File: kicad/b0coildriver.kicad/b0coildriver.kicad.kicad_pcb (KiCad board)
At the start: 2 copper layers, 100.3 x 72.4 mm, 42 parts, among them J1 Vctrl, J2 PSU, J3 COIL, J4 Screw_Terminal_01x04, J5 ISense, U1 LM358, U2 OPA549T, U3 74HC04, U4 CMS2005

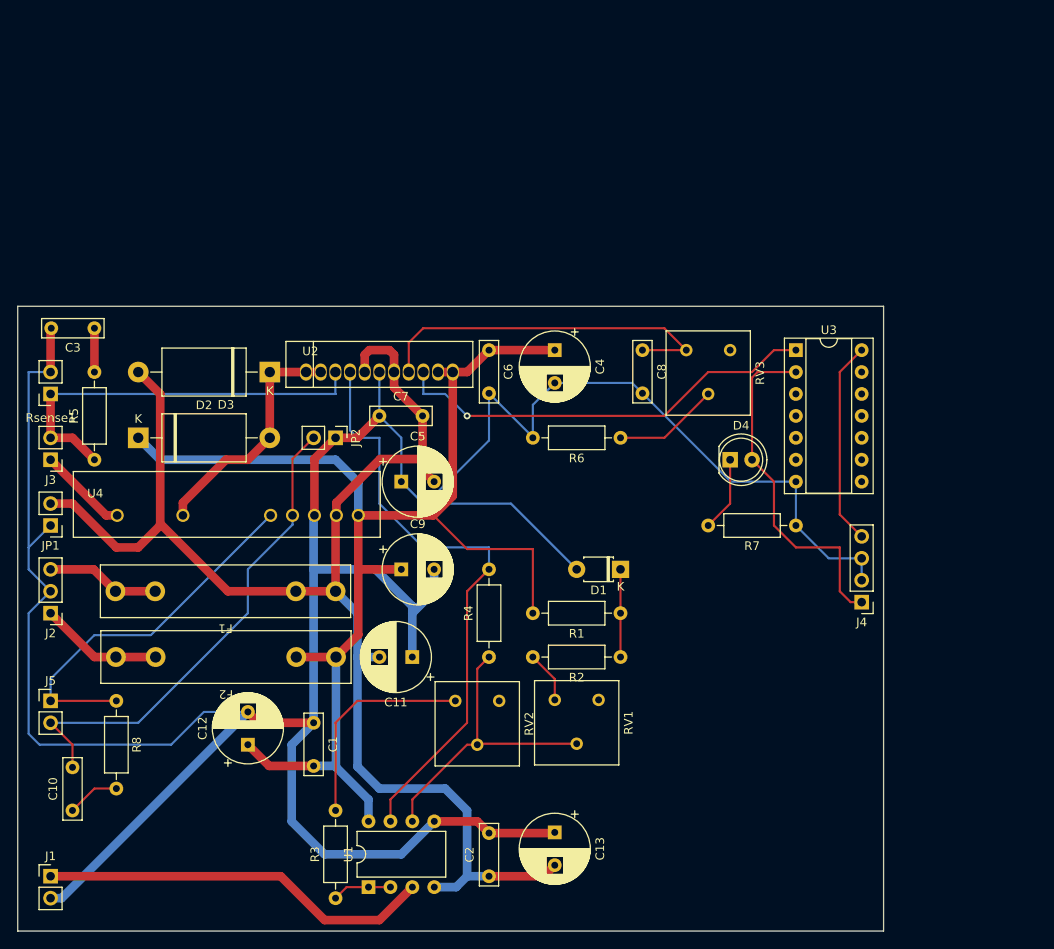
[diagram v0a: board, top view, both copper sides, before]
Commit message: Updated board layout to new feedback network
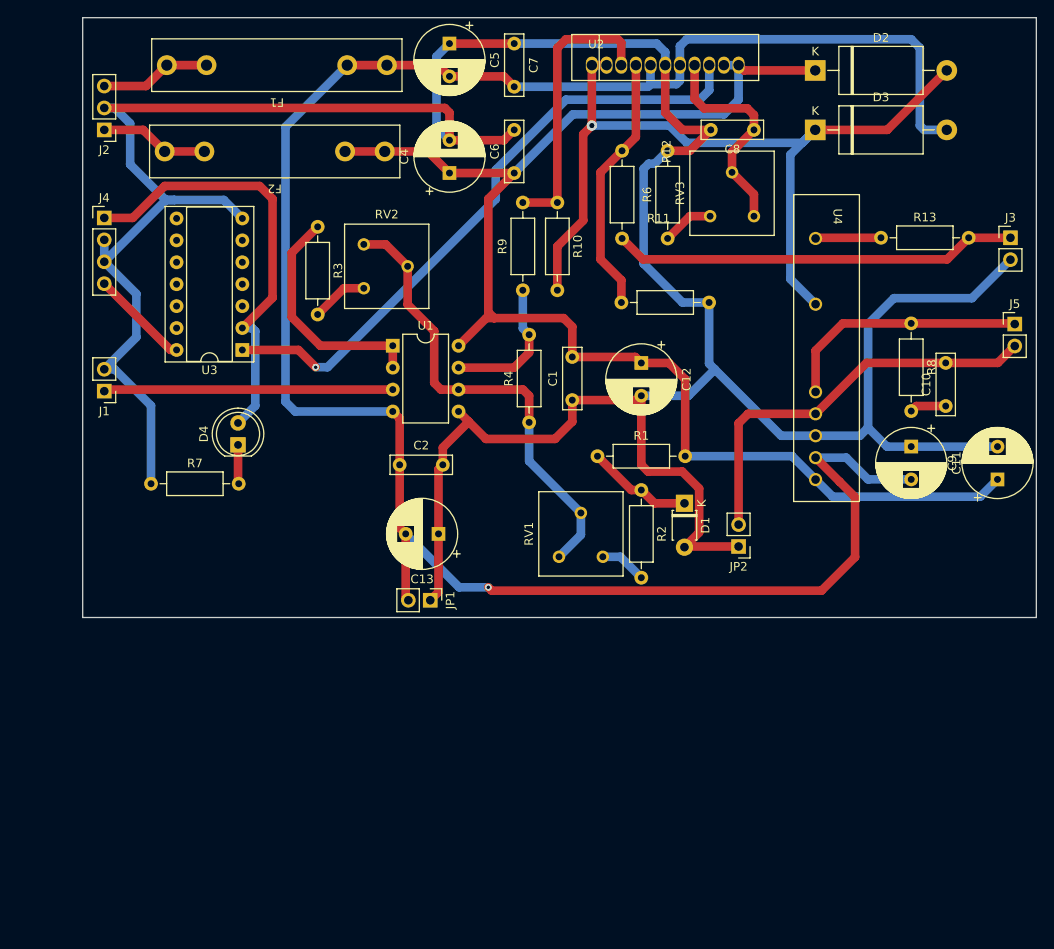
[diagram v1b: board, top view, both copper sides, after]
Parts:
- removed C3: 10nF, Capacitor_THT:C_Rect_L7.0mm_W2.0mm_P5.00mm
- removed R5: 10R, Resistor_THT:R_Axial_DIN0207_L6.3mm_D2.5mm_P10.16mm_Horizontal
- removed Rsense1: 1R, Connector_PinSocket_2.54mm:PinSocket_1x02_P2.54mm_Vertical
- added R10: 10k, Resistor_THT:R_Axial_DIN0207_L6.3mm_D2.5mm_P10.16mm_Horizontal, F.Cu at (140.0, 15.9)
- added R11: 20k, Resistor_THT:R_Axial_DIN0207_L6.3mm_D2.5mm_P10.16mm_Horizontal, F.Cu at (157.6, 27.5)
- added R12: 10k, Resistor_THT:R_Axial_DIN0207_L6.3mm_D2.5mm_P10.16mm_Horizontal, F.Cu at (147.5, 9.92)
- added R13: 1R, Resistor_THT:R_Axial_DIN0207_L6.3mm_D2.5mm_P10.16mm_Horizontal, F.Cu at (177.5, 20.0)
- added R9: 20k, Resistor_THT:R_Axial_DIN0207_L6.3mm_D2.5mm_P10.16mm_Horizontal, F.Cu at (136.0, 26.1)
- moved J5 119.9 mm to (193.0, 30.0)
- moved J3 114.2 mm to (192.5, 20.0), turned to 0 degrees
- moved C10 111.5 mm to (185.0, 39.5)
- moved R8 102.0 mm to (181.0, 29.9)
- moved J4 98.4 mm to (87.5, 17.7), turned to 0 degrees
- moved U4 96.6 mm to (175.0, 15.0), turned to -90 degrees
- moved D2 89.2 mm to (169.9, 0.61)
- moved R3 77.8 mm to (112.2, 18.7), turned to -90 degrees
- moved R7 74.9 mm to (92.9, 48.5), turned to 0 degrees
- moved C9 69.9 mm to (191.0, 48.0), turned to 90 degrees
- moved D3 69.1 mm to (169.9, 7.50), turned to 0 degrees
- moved U3 64.1 mm to (103.5, 33.0), turned to 180 degrees
- moved C12 63.5 mm to (149.7, 34.5), turned to -90 degrees
- moved U1 62.8 mm to (120.9, 32.5), turned to 0 degrees
- moved C11 62.7 mm to (181.0, 44.2), turned to -90 degrees
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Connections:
- C1 pad 1: GND -> VOut-
- C11 pad 1: GND -> VOut-
- C12 pad 2: GND -> VOut-
- C13 pad 1: GND -> VOut-
- C2 pad 2: GND -> VOut-
- C4 pad 2: GND -> VOut-
- C5 pad 1: GND -> VOut-
- C6 pad 2: GND -> VOut-
- C7 pad 1: GND -> VOut-
- C8 pad 2: GND -> VOut-
- C9 pad 2: GND -> VOut-
- D1 pad 2: GND -> VOut-
- J1 pad 2: GND -> VOut-
- J2 pad 2: GND -> VOut-
- J4 pad 2: GND -> VOut-
- J4 pad 3: GND -> VOut-
- JP1 pad 1: GND -> VOut-
- JP2 pad 1: GND -> VOut-
- R4 pad 1: Net-(R4-Pad1) -> Net-(RV1-Pad3)
- R6 pad 1: Net-(R6-Pad1) -> Net-(RV3-Pad3)
- R6 pad 2: GND -> VOut-
- R7 pad 1: GND -> VOut-
- RV1 pad 2: Net-(R4-Pad1) -> Net-(RV1-Pad3)
- RV1 pad 3: unconnected-(RV1-Pad3) -> Net-(RV1-Pad3)
- RV2 pad 2: Net-(R4-Pad1) -> Net-(RV1-Pad3)
- RV2 pad 3: unconnected-(RV2-Pad3) -> Net-(RV1-Pad3)
- RV3 pad 2: Net-(R6-Pad1) -> Net-(C8-Pad1)
- RV3 pad 3: unconnected-(RV3-Pad3) -> Net-(RV3-Pad3)
- U1 pad 5: GND -> VOut-
- U1 pad 6: Net-(R4-Pad1) -> Net-(RV1-Pad3)
- U2 pad 3: VOut- -> Net-(R10-Pad1)
- U2 pad 4: Net-(R4-Pad2) -> Net-(R11-Pad2)
- U2 pad 6: GND -> VOut-
- U3 pad 7: GND -> VOut-
- U4 pad 3: GND -> VOut-
- U4 pad 7: VOut+ -> Net-(R13-Pad1)
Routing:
- net GND: track 353.1 -> 0.00 mm
- net VOut-: track 46.8 -> 366.8 mm
- net -15V: track 164.5 -> 246.4 mm, vias 0 -> 1
- net Net-(D2-Pad2): track 27.3 -> 97.5 mm, vias 0 -> 1
- net Net-(RV1-Pad3): track 0.00 -> 54.7 mm
- net Net-(R4-Pad2): track 69.4 -> 16.4 mm
- net VOut+: track 10.4 -> 47.0 mm
- net Net-(R4-Pad1): track 35.0 -> 0.00 mm
- net Net-(R10-Pad1): track 0.00 -> 32.5 mm
- net Net-(R11-Pad2): track 0.00 -> 30.2 mm
- net Net-(U2-Pad9): track 49.9 -> 73.1 mm
- net Net-(R3-Pad1): track 6.89 -> 27.3 mm
- net Net-(R3-Pad2): track 25.1 -> 6.60 mm
- net Net-(C8-Pad1): track 42.4 -> 25.4 mm
- net Net-(J5-Pad1): track 43.5 -> 29.2 mm
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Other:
- board size 100.3 x 72.4 mm -> 110.5 x 69.5 mm
